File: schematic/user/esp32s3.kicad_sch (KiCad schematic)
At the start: 17 parts, among them J4 I2C Breakout, J6 ESP32_UART0, J7 MCU Power, J8 ULP Serial, SW1 ESP32S3 Reset, SW2 ESP32S3 Boot Method, U5 ESP32-S3-WROOM-1-N16R8

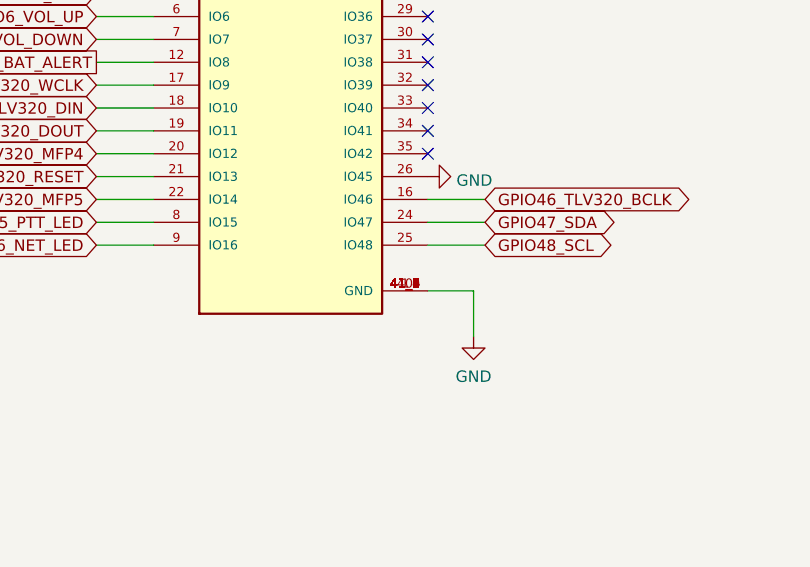
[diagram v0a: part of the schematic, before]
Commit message: v0.7 board: optimize component selection for USB input filter.
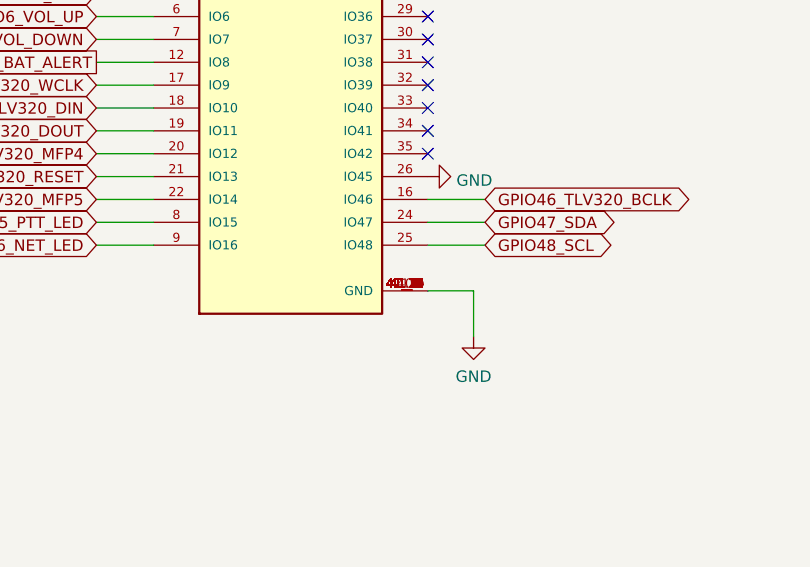
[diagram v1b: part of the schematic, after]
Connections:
- net GND: now also U5.41_10 (GND), U5.41_11 (GND), U5.41_12 (GND), U5.41_13 (GND), U5.41_14 (GND), U5.41_15 (GND), U5.41_16 (GND), U5.41_17 (GND), U5.41_18 (GND), U5.41_19 (GND), U5.41_20 (GND), U5.41_21 (GND)
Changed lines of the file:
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@@
     (pin "40")
     (pin "41_1")
+    (pin "41_20")
+    (pin "41_19")
+    (pin "41_18")
+    (pin "41_17")
+    (pin "41_16")
+    (pin "41_15")
+    (pin "41_14")
+    (pin "41_13")
+    (pin "41_12")
+    (pin "41_11")
+    (pin "41_10")
+    (pin "41_21")
     (pin "41_2")
     (pin "41_3")
